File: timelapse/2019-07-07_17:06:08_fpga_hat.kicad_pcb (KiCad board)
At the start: 4 copper layers, 65 x 56.5 mm, 92 parts, among them J1 2x20, J2 AudioJack3, J3 Conn_02x06_Top_Bottom, J4 Conn_02x06_Top_Bottom, J5 Conn_02x06_Top_Bottom, J6 Conn_01x02, SW1 PTS815, SW2 PTS815, SW3 PTS815, SW4 PTS815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

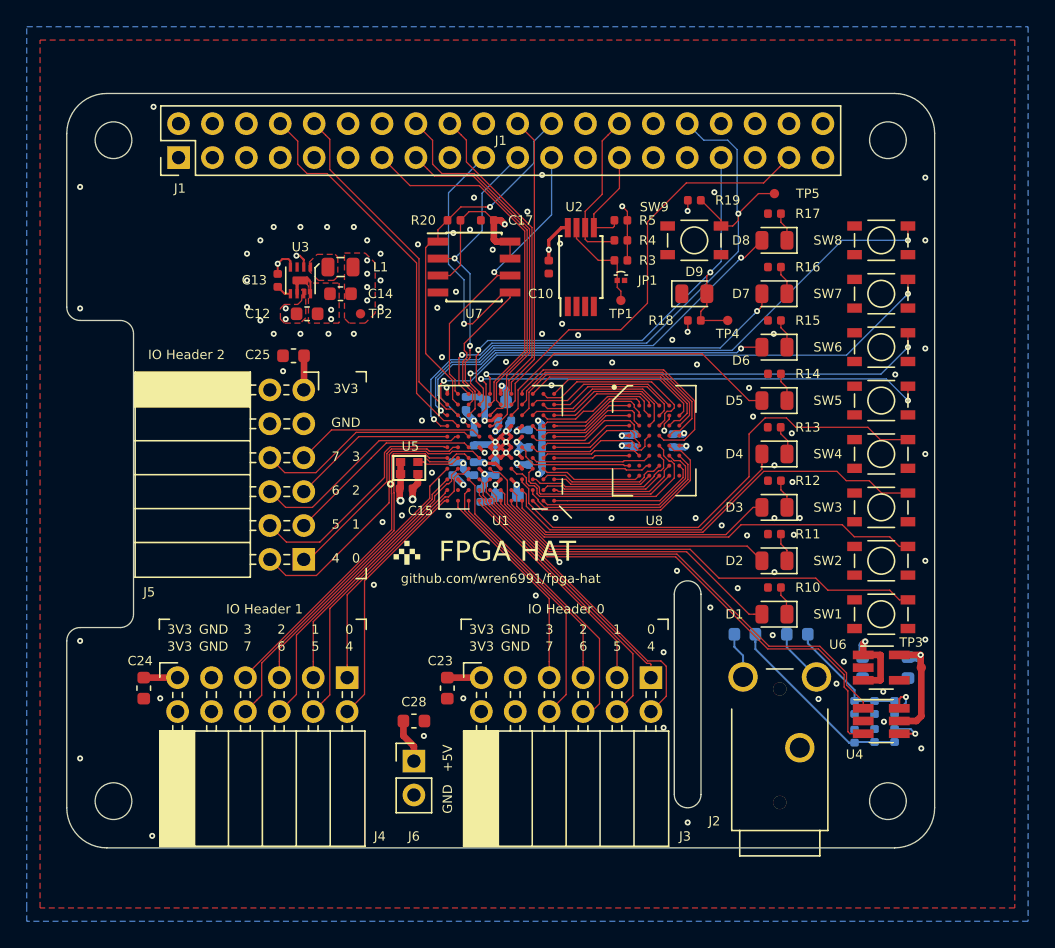
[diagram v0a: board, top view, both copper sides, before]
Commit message: Fix small silkscreen error, improve ground stitching and core supply layout
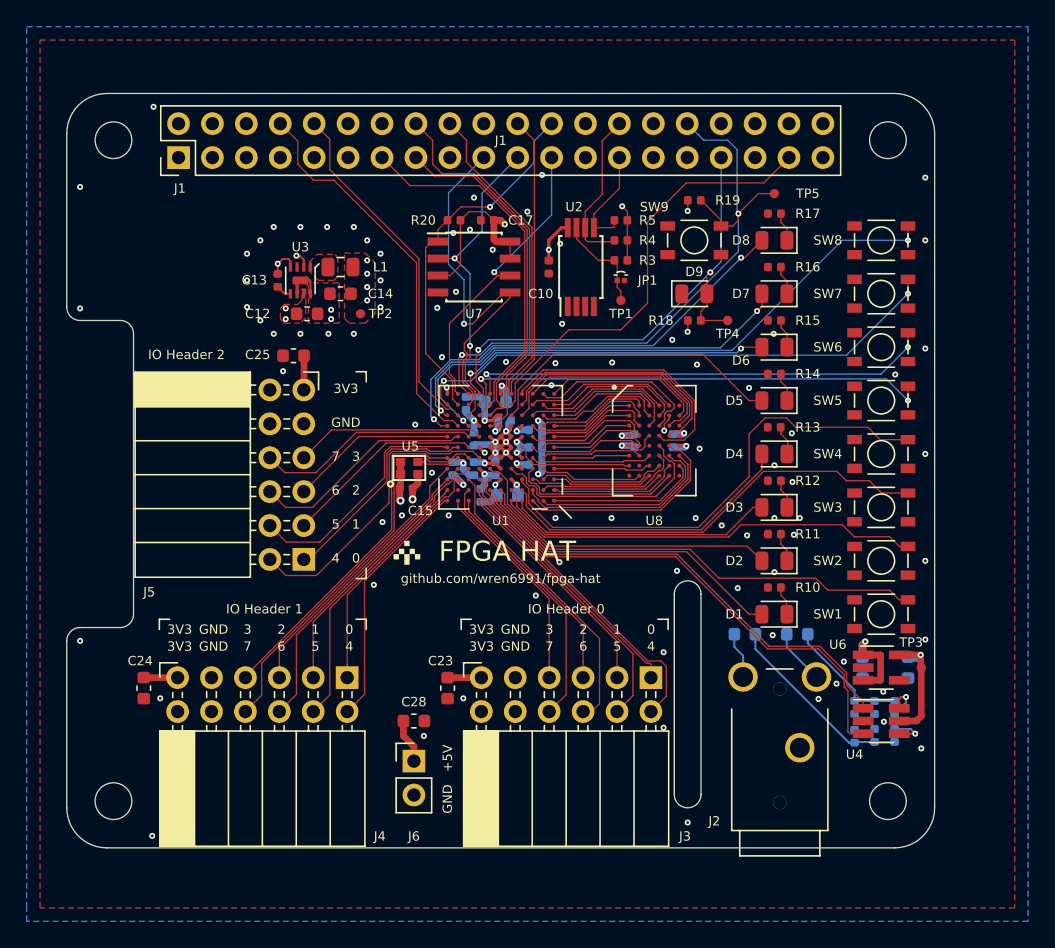
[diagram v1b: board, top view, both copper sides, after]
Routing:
- net GND: vias 106 -> 99
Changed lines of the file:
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@@
     (thickness 1.6)
     (drawings 74)
-    (tracks 1244)
+    (tracks 1237)
     (zones 0)
     (modules 92)
@@
     (37 F.SilkS user)
     (38 B.Mask user hide)
-    (39 F.Mask user)
+    (39 F.Mask user hide)
     (40 Dwgs.User user)
     (41 Cmts.User user)
@@
   )
   (module Capacitor_SMD:C_0603_1608Metric (layer F.Cu)
-    (at 128.5 124.5363 270)
+    (at 128.524 124.5363 270)
     (descr "Capacitor SMD 0603 (1608 Metric), square (rectangular) end terminal, IPC_7351 nominal, (Body size source: http://www.tortai-tech.com/upload/download/2011102023233369053.pdf), generated with kicad-footprint-generator")
     (tags capacitor)
@@
   (segment (start 117.25 94.25) (end 117.5 94) (width 0.25) (layer F.Cu) (net 1))
   (segment (start 117.25 95) (end 117.25 94.25) (width 0.25) (layer F.Cu) (net 1))
-  (via (at 126.6 104.5) (size 0.45) (drill 0.2) (layers F.Cu B.Cu) (net 1) (status 40000))
+  (via (at 126.1 104.8) (size 0.45) (drill 0.2) (layers F.Cu B.Cu) (net 1) (status 40000))
   (via (at 128.6 111.6) (size 0.45) (drill 0.2) (layers F.Cu B.Cu) (net 1) (status 40000))
   (via (at 135.128 117.602) (size 0.45) (drill 0.2) (layers F.Cu B.Cu) (net 1) (status 40000))
@@
   (via (at 114.5 97) (size 0.45) (drill 0.2) (layers F.Cu B.Cu) (net 1))
   (via (at 122.5 91) (size 0.45) (drill 0.2) (layers F.Cu B.Cu) (net 1))
-  (via (at 126.3 91.3) (size 0.45) (drill 0.2) (layers F.Cu B.Cu) (net 1))
-  (via (at 135.6 98) (size 0.45) (drill 0.2) (layers F.Cu B.Cu) (net 1) (status 40000))
-  (via (at 138.3 98.1) (size 0.45) (drill 0.2) (layers F.Cu B.Cu) (net 1) (status 40000))
-  (via (at 148.5 87.4) (size 0.45) (drill 0.2) (layers F.Cu B.Cu) (net 1) (status 40000))
-  (via (at 148.2 118.5) (size 0.45) (drill 0.2) (layers F.Cu B.Cu) (net 1) (status 40000))
-  (via (at 101 129.8) (size 0.45) (drill 0.2) (layers F.Cu B.Cu) (net 1) (status 40000))
-  (via (at 151.4 104.2) (size 0.45) (drill 0.2) (layers F.Cu B.Cu) (net 1) (status 40000))
   (via (at 122.5 92.5) (size 0.45) (drill 0.2) (layers F.Cu B.Cu) (net 2))
   (via (at 133.7 105.3) (size 0.45) (drill 0.2) (layers F.Cu B.Cu) (net 2))
@@
   (segment (start 108.2988 123.7488) (end 108.3 123.75) (width 0.5) (layer F.Cu) (net 7))
   (segment (start 105.7656 123.7488) (end 108.2988 123.7488) (width 0.5) (layer F.Cu) (net 7))
+  (segment (start 131.0488 123.7488) (end 131.05 123.75) (width 0.5) (layer F.Cu) (net 7))
+  (segment (start 128.524 123.7488) (end 131.0488 123.7488) (width 0.5) (layer F.Cu) (net 7))
   (via (at 141.574998 106.375) (size 0.45) (drill 0.2) (layers F.Cu B.Cu) (net 7))
   (segment (start 142.125 106.375) (end 141.574998 106.375) (width 0.15) (layer F.Cu) (net 7))
@@
   (via (at 146.235794 105.44514) (size 0.45) (drill 0.2) (layers F.Cu B.Cu) (net 7))
   (segment (start 145.875 105.625) (end 146.05486 105.44514) (width 0.15) (layer F.Cu) (net 7))
-  (segment (start 131.0488 123.7488) (end 131.05 123.75) (width 0.5) (layer F.Cu) (net 7))
-  (segment (start 128.524 123.7488) (end 131.0488 123.7488) (width 0.5) (layer F.Cu) (net 7))
   (via (at 116.4 96.1) (size 0.45) (drill 0.2) (layers F.Cu B.Cu) (net 8))
   (segment (start 126 128.89375) (end 126 130) (width 0.5) (layer F.Cu) (net 8))
@@
   (segment (start 130.665646 101.553232) (end 130.665646 99.6797) (width 0.09) (layer F.Cu) (net 31))
   (segment (start 130.665646 99.6797) (end 130.818249 99.527097) (width 0.09) (layer F.Cu) (net 31))
-  (segment (start 143.1 98.5) (end 148.2 93.4) (width 0.09) (layer B.Cu) (net 31))
-  (segment (start 130.818249 99.208899) (end 131.527148 98.5) (width 0.09) (layer B.Cu) (net 31))
-  (segment (start 131.527148 98.5) (end 143.1 98.5) (width 0.09) (layer B.Cu) (net 31))
-  (segment (start 128.9 104.5) (end 129.3 104.9) (width 0.09) (layer F.Cu) (net 35))
+  (segment (start 143.161426 98.438574) (end 148.2 93.4) (width 0.09) (layer B.Cu) (net 31))
+  (segment (start 131.588574 98.438574) (end 143.161426 98.438574) (width 0.09) (layer B.Cu) (net 31))
+  (segment (start 130.818249 99.208899) (end 131.588574 98.438574) (width 0.09) (layer B.Cu) (net 31))
   (segment (start 128.236262 104.5) (end 128.9 104.5) (width 0.09) (layer F.Cu) (net 35))
   (segment (start 126.2 102.463738) (end 128.236262 104.5) (width 0.09) (layer F.Cu) (net 35))
-  (segment (start 117.3 83.57) (end 117.3 85.3) (width 0.09) (layer F.Cu) (net 35))
+  (segment (start 128.9 104.5) (end 129.3 104.9) (width 0.09) (layer F.Cu) (net 35))
   (segment (start 115.99 82.26) (end 117.3 83.57) (width 0.09) (layer F.Cu) (net 35))
-  (segment (start 117.3 85.3) (end 118 86) (width 0.09) (layer F.Cu) (net 35))
-  (segment (start 118 86) (end 119.5 86) (width 0.09) (layer F.Cu) (net 35))
-  (segment (start 119.5 86) (end 126.2 92.7) (width 0.09) (layer F.Cu) (net 35))
+  (segment (start 117.3 83.57) (end 117.3 85.3) (width 0.09) (layer F.Cu) (net 35))
+  (segment (start 117.3 85.3) (end 118.5 86.5) (width 0.09) (layer F.Cu) (net 35))
+  (segment (start 118.5 86.5) (end 120 86.5) (width 0.09) (layer F.Cu) (net 35))
   (segment (start 126.2 92.7) (end 126.2 102.463738) (width 0.09) (layer F.Cu) (net 35))
+  (segment (start 120 86.5) (end 126.2 92.7) (width 0.09) (layer F.Cu) (net 35))
   (segment (start 119.379999 83.109999) (end 118.53 82.26) (width 0.09) (layer F.Cu) (net 36))
   (segment (start 128.834988 103.634988) (end 128.413186 103.634988) (width 0.09) (layer F.Cu) (net 36))
